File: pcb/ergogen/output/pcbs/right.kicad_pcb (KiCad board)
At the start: 2 copper layers, 136.9 x 74.7 mm, 57 parts, among them J1 JST_SH_BM06B-SRSS-TB_1x06-1MP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

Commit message: Check the hotswap sockets on the PCB underside; move connectors clear of them
The socket footprints sit on the front layer, so the back-side checks skipped
them. Now the socket bodies are modeled and checked against nuts, connectors,
posts, poron, battery, screens, ball unit and switch cover (also at full PCB travel).

- Battery connectors (left/right) and the sensor connector J1 moved into free spots
- Tray rim trimmed under the outer-column sockets at the top-right corner

Co-Authored-By: Claude Opus 5.5 <noreply@anthropic.com>
Claude-Session: https://claude.ai/code/session_017zNm7dMSTHELcztuNr6aNy
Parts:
- moved BAT1 26.9 mm to (267.0, -10.0), turned to 0 degrees
- moved J1 20.6 mm to (247.0, -29.0), turned to 180 degrees
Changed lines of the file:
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@@
     )
       (module "Connector_JST:JST_SH_BM06B-SRSS-TB_1x06-1MP_P1.00mm_Vertical" (layer B.Cu)
-      (at 238.10000000000002 -10.400000000000006 0)
-      (fp_text reference "J1" (at 0 3.3 0) (layer B.SilkS) hide (effects (font (size 1 1) (thickness 0.15)) (justify mirror)))
-      (fp_text value "JST_SH_BM06B-SRSS-TB_1x06-1MP_P1.00mm_Vertical" (at 0 0 0) (layer B.Fab) hide (effects (font (size 0.8 0.8) (thickness 0.12)) (justify mirror)))
+      (at 247 -29.000000000000007 180)
+      (fp_text reference "J1" (at 0 3.3 180) (layer B.SilkS) hide (effects (font (size 1 1) (thickness 0.15)) (justify mirror)))
+      (fp_text value "JST_SH_BM06B-SRSS-TB_1x06-1MP_P1.00mm_Vertical" (at 0 0 180) (layer B.Fab) hide (effects (font (size 0.8 0.8) (thickness 0.12)) (justify mirror)))
       (fp_line (start -4.11 0.04) (end -4.11 -1.11) (layer B.SilkS) (width 0.12))
       (fp_line (start -4.11 -1.11) (end -3.06 -1.11) (layer B.SilkS) (width 0.12))
@@
 (fp_line (start 2.65 0.95) (end 2.35 0.95) (layer B.Fab) (width 0.1))
 (fp_line (start 2.35 0.95) (end 2.35 1.55) (layer B.Fab) (width 0.1))
-      (pad "1" smd roundrect (at -2.5 -1.325 0) (size 0.6 1.55) (roundrect_rratio 0.25) (layers B.Cu B.Mask B.Paste) (net 33 "3V3"))
-      (pad "2" smd roundrect (at -1.5 -1.325 0) (size 0.6 1.55) (roundrect_rratio 0.25) (layers B.Cu B.Mask B.Paste) (net 34 "GND"))
-      (pad "3" smd roundrect (at -0.5 -1.325 0) (size 0.6 1.55) (roundrect_rratio 0.25) (layers B.Cu B.Mask B.Paste) (net 35 "TB_SCLK"))
-      (pad "4" smd roundrect (at 0.5 -1.325 0) (size 0.6 1.55) (roundrect_rratio 0.25) (layers B.Cu B.Mask B.Paste) (net 36 "TB_SDIO"))
-      (pad "5" smd roundrect (at 1.5 -1.325 0) (size 0.6 1.55) (roundrect_rratio 0.25) (layers B.Cu B.Mask B.Paste) (net 37 "TB_NCS"))
-      (pad "6" smd roundrect (at 2.5 -1.325 0) (size 0.6 1.55) (roundrect_rratio 0.25) (layers B.Cu B.Mask B.Paste) (net 38 "TB_MOTION"))
-      (pad "MP" smd roundrect (at -3.8 1.2 0) (size 1.2 1.8) (roundrect_rratio 0.208333) (layers B.Cu B.Mask B.Paste))
-      (pad "MP" smd roundrect (at 3.8 1.2 0) (size 1.2 1.8) (roundrect_rratio 0.208333) (layers B.Cu B.Mask B.Paste))
+      (pad "1" smd roundrect (at -2.5 -1.325 180) (size 0.6 1.55) (roundrect_rratio 0.25) (layers B.Cu B.Mask B.Paste) (net 33 "3V3"))
+      (pad "2" smd roundrect (at -1.5 -1.325 180) (size 0.6 1.55) (roundrect_rratio 0.25) (layers B.Cu B.Mask B.Paste) (net 34 "GND"))
+      (pad "3" smd roundrect (at -0.5 -1.325 180) (size 0.6 1.55) (roundrect_rratio 0.25) (layers B.Cu B.Mask B.Paste) (net 35 "TB_SCLK"))
+      (pad "4" smd roundrect (at 0.5 -1.325 180) (size 0.6 1.55) (roundrect_rratio 0.25) (layers B.Cu B.Mask B.Paste) (net 36 "TB_SDIO"))
+      (pad "5" smd roundrect (at 1.5 -1.325 180) (size 0.6 1.55) (roundrect_rratio 0.25) (layers B.Cu B.Mask B.Paste) (net 37 "TB_NCS"))
+      (pad "6" smd roundrect (at 2.5 -1.325 180) (size 0.6 1.55) (roundrect_rratio 0.25) (layers B.Cu B.Mask B.Paste) (net 38 "TB_MOTION"))
+      (pad "MP" smd roundrect (at -3.8 1.2 180) (size 1.2 1.8) (roundrect_rratio 0.208333) (layers B.Cu B.Mask B.Paste))
+      (pad "MP" smd roundrect (at 3.8 1.2 180) (size 1.2 1.8) (roundrect_rratio 0.208333) (layers B.Cu B.Mask B.Paste))
       (model "${KICAD10_3DMODEL_DIR}/Connector_JST.3dshapes/JST_SH_BM06B-SRSS-TB_1x06-1MP_P1.00mm_Vertical.step")
       )
@@
       )
       (module "Connector_Molex:Molex_PicoBlade_53261-0271_1x02-1MP_P1.25mm_Horizontal" (layer B.Cu)
-      (at 286 -29 -90)
-      (fp_text reference "BAT1" (at 0 4.4 -90) (layer B.SilkS) hide (effects (font (size 1 1) (thickness 0.15)) (justify mirror)))
-      (fp_text value "Molex_PicoBlade_53261-0271_1x02-1MP_P1.25mm_Horizontal" (at 0 0 -90) (layer B.Fab) hide (effects (font (size 0.8 0.8) (thickness 0.12)) (justify mirror)))
+      (at 267 -10 0)
+      (fp_text reference "BAT1" (at 0 4.4 0) (layer B.SilkS) hide (effects (font (size 1 1) (thickness 0.15)) (justify mirror)))
+      (fp_text value "Molex_PicoBlade_53261-0271_1x02-1MP_P1.25mm_Horizontal" (at 0 0 0) (layer B.Fab) hide (effects (font (size 0.8 0.8) (thickness 0.12)) (justify mirror)))
       (fp_line (start -2.235 1.71) (end -1.285 1.71) (layer B.SilkS) (width 0.12))
       (fp_line (start -2.235 1.26) (end -2.235 1.71) (layer B.SilkS) (width 0.12))
@@
       (fp_line (start 3.825 0.4) (end 3.825 -1.4) (layer B.Fab) (width 0.1))
       (fp_line (start 3.825 -1.4) (end 3.625 -1.6) (layer B.Fab) (width 0.1))
-      (pad "1" smd roundrect (at -0.625 2.4 -90) (size 0.8 1.6) (roundrect_rratio 0.25) (layers B.Cu B.Mask B.Paste) (net 34 "GND"))
-      (pad "2" smd roundrect (at 0.625 2.4 -90) (size 0.8 1.6) (roundrect_rratio 0.25) (layers B.Cu B.Mask B.Paste) (net 43 "BAT_P"))
-      (pad "MP" smd roundrect (at -3.175 -0.5 -90) (size 2.1 3) (roundrect_rratio 0.119048) (layers B.Cu B.Mask B.Paste))
-      (pad "MP" smd roundrect (at 3.175 -0.5 -90) (size 2.1 3) (roundrect_rratio 0.119048) (layers B.Cu B.Mask B.Paste))
+      (pad "1" smd roundrect (at -0.625 2.4 0) (size 0.8 1.6) (roundrect_rratio 0.25) (layers B.Cu B.Mask B.Paste) (net 34 "GND"))
+      (pad "2" smd roundrect (at 0.625 2.4 0) (size 0.8 1.6) (roundrect_rratio 0.25) (layers B.Cu B.Mask B.Paste) (net 43 "BAT_P"))
+      (pad "MP" smd roundrect (at -3.175 -0.5 0) (size 2.1 3) (roundrect_rratio 0.119048) (layers B.Cu B.Mask B.Paste))
+      (pad "MP" smd roundrect (at 3.175 -0.5 0) (size 2.1 3) (roundrect_rratio 0.119048) (layers B.Cu B.Mask B.Paste))
       (model "${KICAD10_3DMODEL_DIR}/Connector_Molex.3dshapes/Molex_PicoBlade_53261-0271_1x02-1MP_P1.25mm_Horizontal.step")
       )

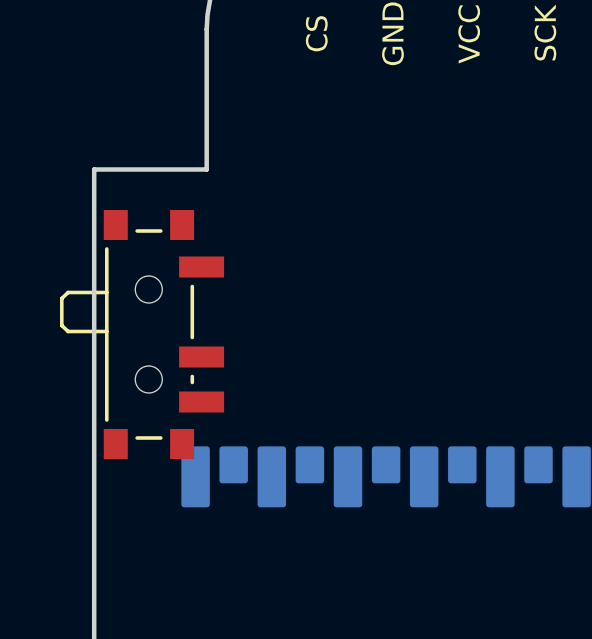
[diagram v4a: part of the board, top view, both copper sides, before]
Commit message: Ukishima: full PCB parts list and height stack; fix clashes it revealed
- check_pcb reads KiCad 8 footprints too (the encoder was skipped): the post
  under the encoder pins moved to a free spot under the encoder
- All back-side parts (XIAO, connectors, SOD-123 diodes, nuts, trimmed pins,
  sockets) are modeled with heights and checked at full PCB travel
- PCB raised 0.3mm so a thicker battery (+0.3) still clears the sockets
- Tray wall recessed under the XIAO end; power switch moved 1mm back so its
  cover clears the XIAO
- nice!view height from a standard 2.5mm pin header; switch cover heights follow the PCB
- docs: parts table (incl. no resistors needed) and height stack

Co-Authored-By: Claude Opus 5.5 <noreply@anthropic.com>
Claude-Session: https://claude.ai/code/session_017zNm7dMSTHELcztuNr6aNy
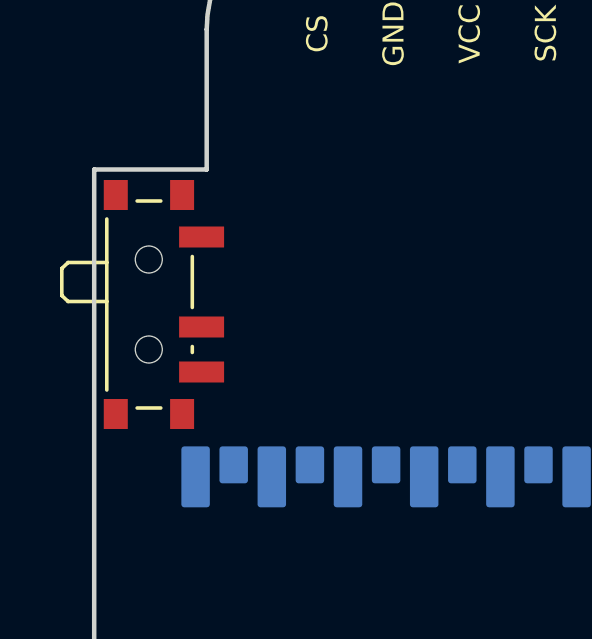
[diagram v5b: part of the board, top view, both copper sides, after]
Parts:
- moved PWR1 1.00 mm to (189.6, -52.5)
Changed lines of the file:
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@@
       )
       (module "Button_Switch_SMD:SW_SPDT_PCM12" (layer F.Cu)
-      (at 189.625 -51.50000000000001 -90)
+      (at 189.625 -52.50000000000001 -90)
       (fp_text reference "PWR1" (at 0 -3.2 -90) (layer F.SilkS) hide (effects (font (size 1 1) (thickness 0.15)) ))
       (fp_text value "SW_SPDT_PCM12" (at 0 0 -90) (layer F.Fab) hide (effects (font (size 0.8 0.8) (thickness 0.12)) ))
